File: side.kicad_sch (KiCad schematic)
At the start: 52 parts, among them SW1 SW_Push, SW10 SW_Push, SW11 SW_Push, SW12 SW_Push, SW13 SW_Push, SW14 SW_Push, SW15 SW_Push, SW16 SW_Push, SW17 SW_Push, SW18 SW_Push, SW19 SW_Push, SW2 SW_Push, SW20 SW_Push, SW22 SW_Push, SW3 SW_Push, SW4 SW_Push, SW5 SW_Push, SW6 SW_Push, SW7 SW_Push, SW8 SW_Push, SW9 SW_Push, U1 XIAO-nRF52840-SMD

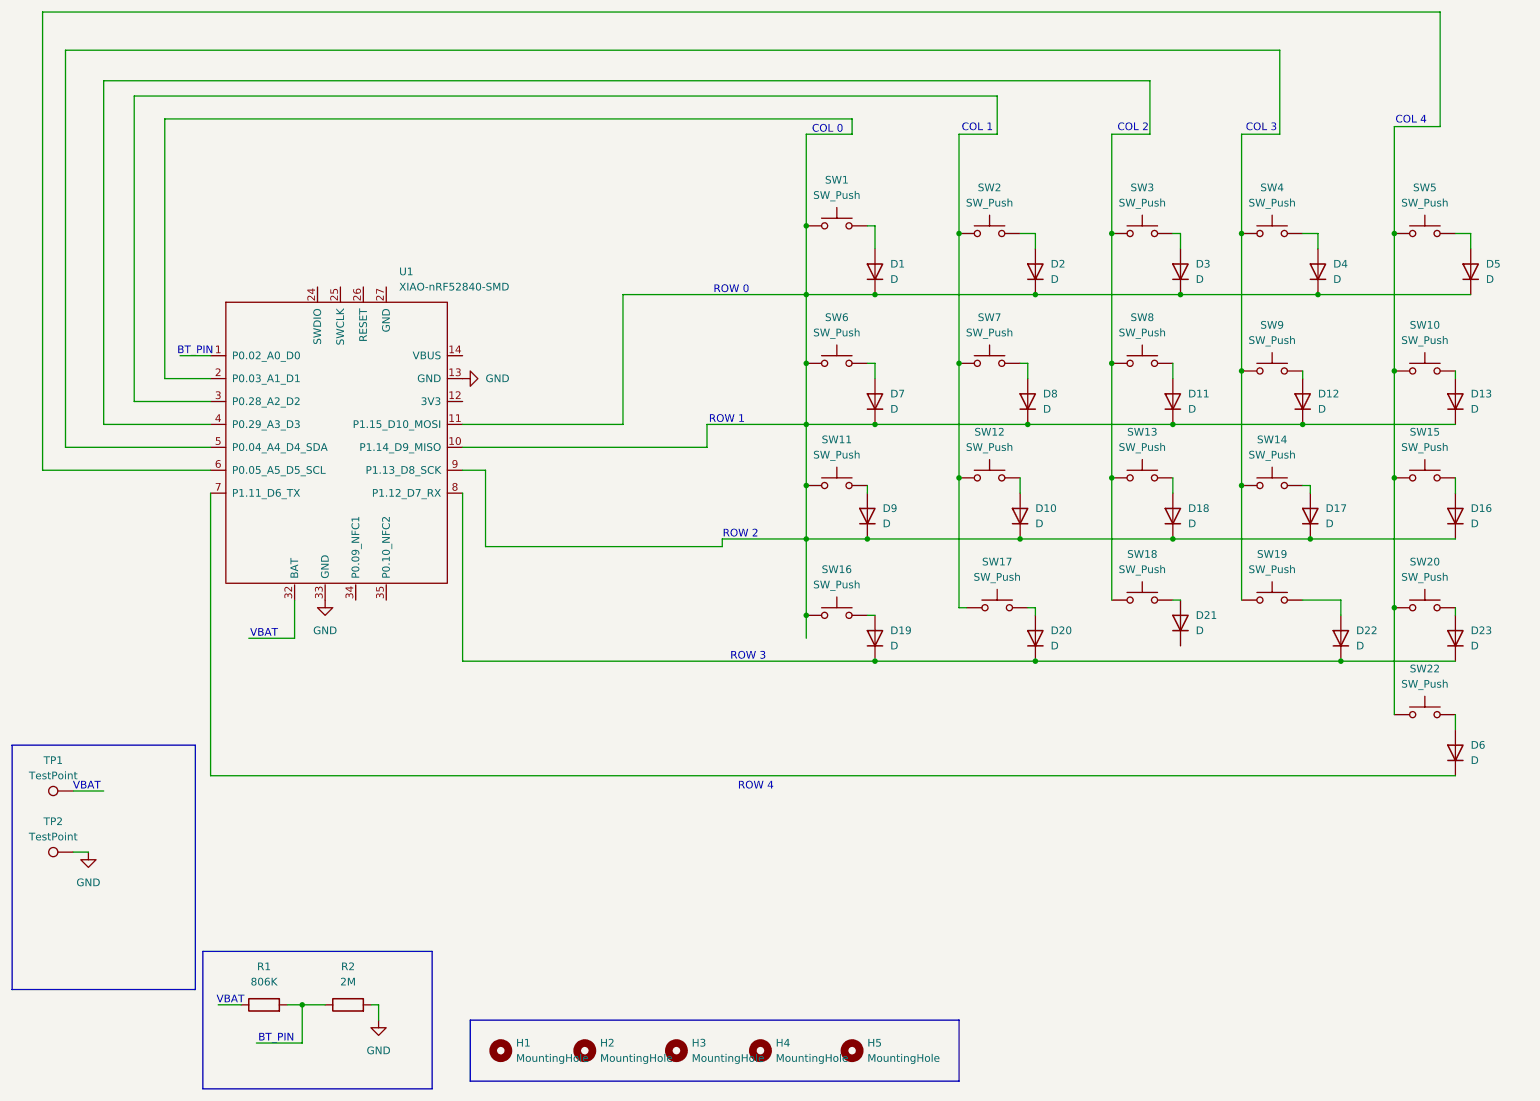
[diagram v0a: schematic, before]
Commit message: Rename schematic halves, update sheets and backups
Rename rightside.kicad_sch -> half.kicad_sch and lefthalf.kicad_sch -> side.kicad_sch; update sheet references, UUIDs, sheetfile names and sheet positions in kronos.kicad_sch and kronos.kicad_pro. Many symbol/text positions, junctions, wires and UUIDs were adjusted in the renamed/updated sheets to reflect the new layout. Clear used_designators in the project file. Rotate backup artifacts: remove two old kronos backups and add three new kronos-backups ZIPs; add ~kronos.kicad_pro.lck. This change reorganizes the schematic halves and updates project metadata and backups accordingly.
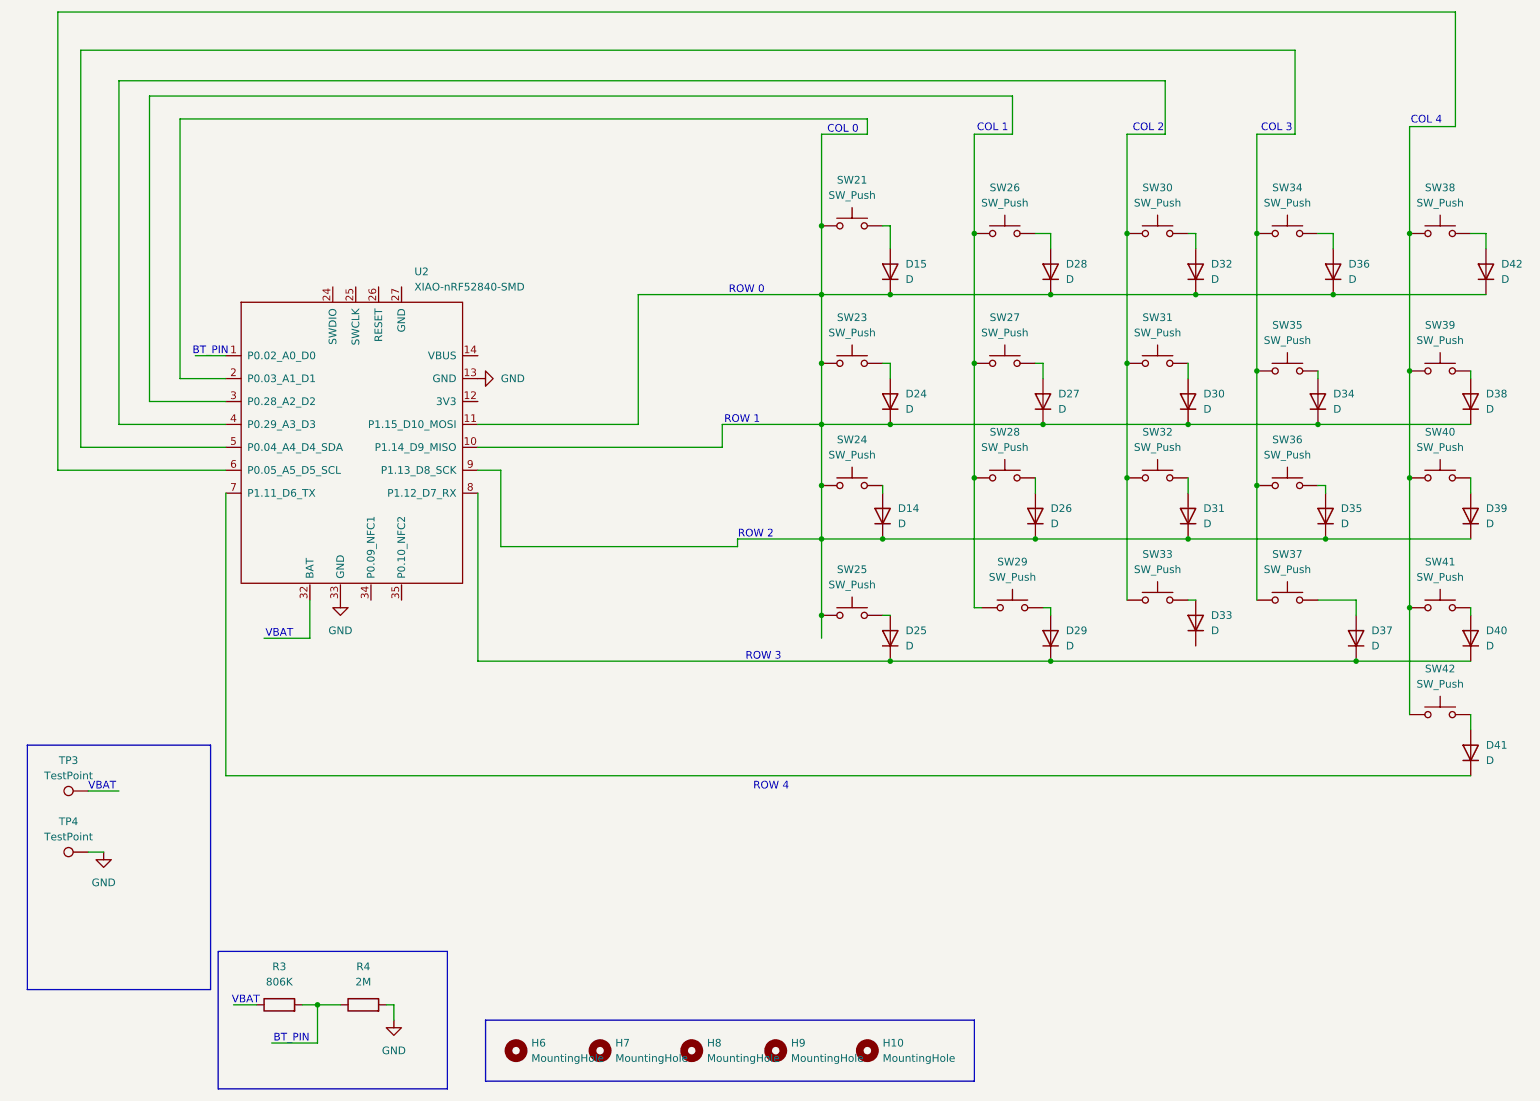
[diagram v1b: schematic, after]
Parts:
- removed D1, D10, D11, D12, D13, D16, D17, D18, D19, D2, D20, D21, D22, D23, D3, D4, D5, D6, D7, D8, D9: D, symbol Device:D
- removed H1, H2, H3, H4, H5: MountingHole, symbol Mechanical:MountingHole
- removed R1: 806K, symbol Device:R
- removed R2: 2M, symbol Device:R
- removed SW1, SW10, SW11, SW12, SW13, SW14, SW15, SW16, SW17, SW18, SW19, SW2, SW20, SW22, SW3, SW4, SW5, SW6, SW7, SW8, SW9: SW_Push, symbol Switch:SW_Push
- removed TP1, TP2: TestPoint, symbol Connector:TestPoint
- removed U1: XIAO-nRF52840-SMD, Seeed_Studio_XIAO_Series:XIAO-nRF52840-SMD, symbol Seeed_Studio_XIAO_Series:XIAO-nRF52840-SMD
- added D14, D15, D24, D25, D26, D27, D28, D29, D30, D31, D32, D33, D34, D35, D36, D37, D38, D39, D40, D41, D42: D, Diode_SMD:D_SOD-123, symbol Device:D
- added H10, H6, H7, H8, H9: MountingHole, symbol Mechanical:MountingHole
- added R3: 806K, Resistor_SMD:R_0805_2012Metric, symbol Device:R
- added R4: 2M, Resistor_SMD:R_0805_2012Metric, symbol Device:R
- added SW21, SW23, SW24, SW25, SW26, SW27, SW28, SW29, SW30, SW31, SW32, SW33, SW34, SW35, SW36, SW37, SW38, SW39, SW40, SW41, SW42: SW_Push, symbol Switch:SW_Push
- added TP3, TP4: TestPoint, TestPoint:TestPoint_Pad_D2.0mm, symbol Connector:TestPoint
- added U2: XIAO-nRF52840-SMD, kronoschems:modified-XIAO-nRF52840-SMD, symbol Seeed_Studio_XIAO_Series:XIAO-nRF52840-SMD
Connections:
- net GND: now also R4.2, TP4.1, U2.13 (GND), U2.33 (GND)
- new net: D14.1 (K), D15.1 (K), D24.1 (K), D26.1 (K), D27.1 (K), D28.1 (K), D30.1 (K), D31.1 (K), D32.1 (K), D34.1 (K), D35.1 (K), D36.1 (K), D38.1 (K), D39.1 (K), D42.1 (K), SW21.1, SW23.1, SW24.1, SW25.1, U2.10 (P1.14_D9_MISO), U2.11 (P1.15_D10_MOSI), U2.2 (P0.03_A1_D1), U2.9 (P1.13_D8_SCK)
- new net: D42.2 (A), SW38.2
- new net: SW34.1, SW35.1, SW36.1, SW37.1, U2.5 (P0.04_A4_D4_SDA)
- new net: D35.2 (A), SW36.2
- new net: D33.2 (A), SW33.2
- new net: D14.2 (A), SW24.2
- new net: SW30.1, SW31.1, SW32.1, SW33.1, U2.4 (P0.29_A3_D3)
- new net: D30.2 (A), SW31.2
- new net: D32.2 (A), SW30.2
- new net: D41.1 (K), U2.7 (P1.11_D6_TX)
- new net: D41.2 (A), SW42.2
- new net: SW26.1, SW27.1, SW28.1, SW29.1, U2.3 (P0.28_A2_D2)
- new net: SW38.1, SW39.1, SW40.1, SW41.1, SW42.1, U2.6 (P0.05_A5_D5_SCL)
- new net: D25.1 (K), D29.1 (K), D37.1 (K), D40.1 (K), U2.8 (P1.12_D7_RX)
- new net: D26.2 (A), SW28.2
- new net: D15.2 (A), SW21.2
- new net: D39.2 (A), SW40.2
- new net: R3.2, R4.1
- new net: D38.2 (A), SW39.2
- new net: D37.2 (A), SW37.2
- new net: D27.2 (A), SW27.2
- new net: D25.2 (A), SW25.2
- new net: D40.2 (A), SW41.2
- new net: D24.2 (A), SW23.2
- new net: D34.2 (A), SW35.2
- new net: D31.2 (A), SW32.2
- new net: D29.2 (A), SW29.2
- new net: D28.2 (A), SW26.2
- new net: D36.2 (A), SW34.2

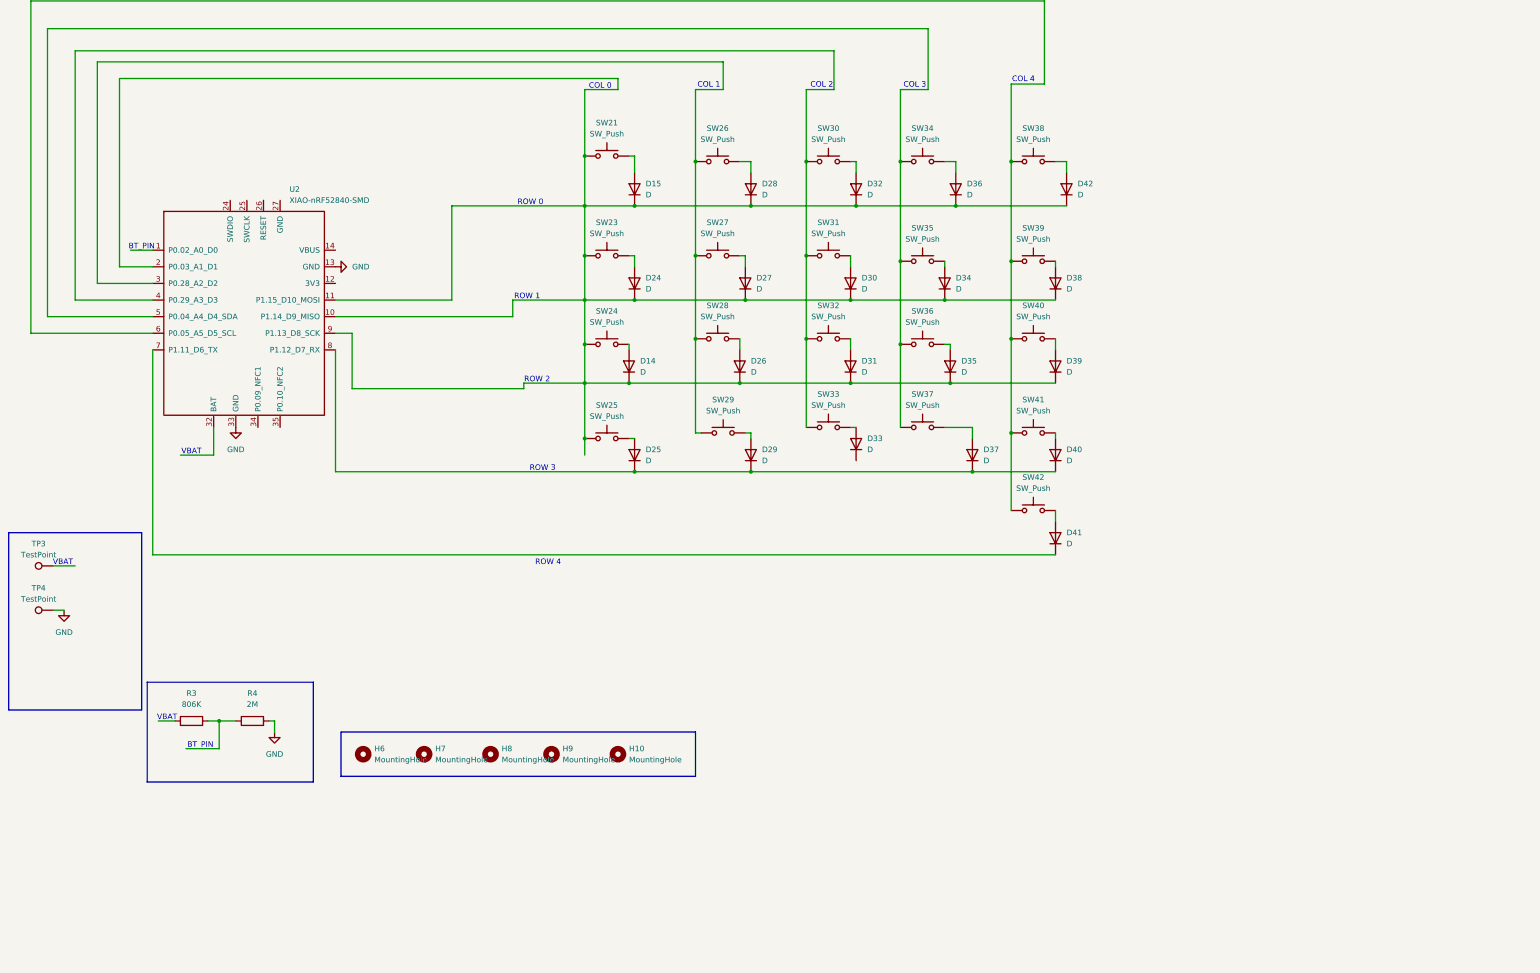
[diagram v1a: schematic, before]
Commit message: Update kronos PCB and add backups
Add 11 kronos backup archives to kronos-backups/ and update kronos.kicad_pcb with expanded PCB data (layers, setup, footprints, pads and components). Also update project files kronos.kicad_prl, kronos.kicad_pro and side.kicad_sch. These changes capture a saved PCB layout revision and store multiple timestamped backups.
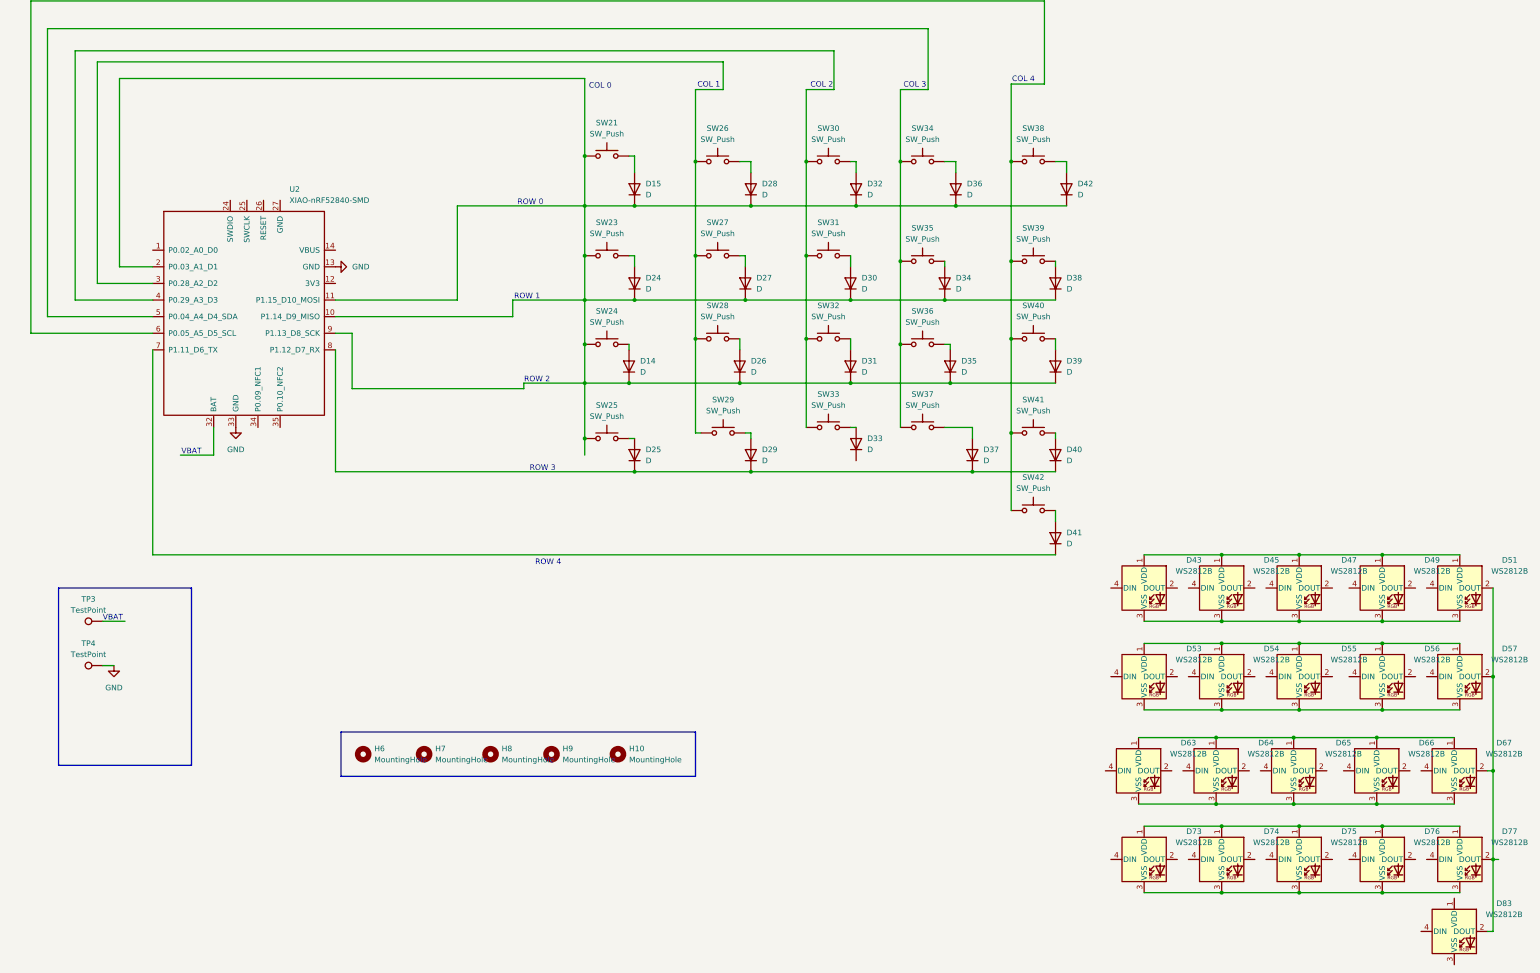
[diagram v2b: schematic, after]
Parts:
- removed R3: 806K, Resistor_SMD:R_0805_2012Metric, symbol Device:R
- removed R4: 2M, Resistor_SMD:R_0805_2012Metric, symbol Device:R
- added D43, D45, D47, D49, D51, D53, D54, D55, D56, D57, D63, D64, D65, D66, D67, D73, D74, D75, D76, D77, D83: WS2812B, LED_SMD:LED_WS2812B_PLCC4_5.0x5.0mm_P3.2mm, symbol LED:WS2812B
- H10, H6, H7, H8, H9: footprint (none) -> kronoschems:mouse-bite-5mm-slot
- SW21, SW23, SW24, SW25, SW26, SW27, SW28, SW29, SW30, SW31, SW32, SW33, SW34, SW35, SW36, SW37, SW38, SW39, SW40, SW41, SW42: footprint (none) -> PCM_marbastlib-mx:SW_MX_HS_KS-2P02B01-01_1u
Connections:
- new net: D53.1 (VDD), D54.1 (VDD), D55.1 (VDD), D56.1 (VDD), D57.1 (VDD)
- new net: D53.3 (VSS), D54.3 (VSS), D55.3 (VSS), D56.3 (VSS), D57.3 (VSS)
- new net: D43.1 (VDD), D45.1 (VDD), D47.1 (VDD), D49.1 (VDD), D51.1 (VDD)
- new net: D43.3 (VSS), D45.3 (VSS), D47.3 (VSS), D49.3 (VSS), D51.3 (VSS)
- new net: D51.2 (DOUT), D57.2 (DOUT), D67.2 (DOUT), D77.2 (DOUT), D83.2 (DOUT)
- new net: D73.1 (VDD), D74.1 (VDD), D75.1 (VDD), D76.1 (VDD), D77.1 (VDD)
- new net: D73.3 (VSS), D74.3 (VSS), D75.3 (VSS), D76.3 (VSS), D77.3 (VSS)
- new net: D63.1 (VDD), D64.1 (VDD), D65.1 (VDD), D66.1 (VDD), D67.1 (VDD)
- new net: D63.3 (VSS), D64.3 (VSS), D65.3 (VSS), D66.3 (VSS), D67.3 (VSS)
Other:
- note removed: "BT_PIN"
- moved on the sheet: TP3, TP4

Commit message: PCB akmost done
PCB added; scheme update; blah blah
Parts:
- removed D43, D45, D47, D49, D51, D53, D54, D55, D56, D57, D63, D64, D65, D66, D67, D73, D74, D75, D76, D77, D83: WS2812B, LED_SMD:LED_WS2812B_PLCC4_5.0x5.0mm_P3.2mm, symbol LED:WS2812B
- removed U2: XIAO-nRF52840-SMD, kronoschems:modified-XIAO-nRF52840-SMD, symbol Seeed_Studio_XIAO_Series:XIAO-nRF52840-SMD
- added D101, D103, D104, D106, D113, D114, D116, D117, D118, D126, D86, D87, D89, D90, D91, D93, D94, D95, D97, D98, D99: WS2812B, LED_SMD:LED_WS2812B_PLCC4_5.0x5.0mm_P3.2mm, symbol LED:WS2812B
- added U3: Seeeduino Xiao nRF52840, PCM_marbastlib-xp-promicroish:Xiao_nRF52840_ACH, symbol PCM_marbastlib-promicroish:Seeeduino_Xiao_nRF52840
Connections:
- net GND: now also D101.3 (VSS), D103.3 (VSS), D104.3 (VSS), D106.3 (VSS), D113.3 (VSS), D114.3 (VSS), D116.3 (VSS), D117.3 (VSS), D118.3 (VSS), D126.3 (VSS), D86.3 (VSS), D87.3 (VSS), D89.3 (VSS), D90.3 (VSS), D91.3 (VSS), D93.3 (VSS), D94.3 (VSS), D95.3 (VSS), D97.3 (VSS), D98.3 (VSS), D99.3 (VSS), U3.15 (BAT-), U3.9 (GND)
- net at D14.1 (K), D15.1 (K), D24.1 (K)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: now also U3.11 (P1.15), U3.12 (P1.14), U3.13 (P1.13), U3.2 (P0.03)
- net at SW34.1, SW35.1, SW36.1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: now also U3.5 (P0.04)
- net at D33.1 (K): now also D25.1 (K), D29.1 (K), D37.1 (K), D40.1 (K), U3.14 (P1.12)
- net at SW30.1, SW31.1, SW32.1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: now also U3.4 (P0.29)
- net at D41.1 (K): now also U3.7 (P1.11)
- net at SW26.1, SW27.1, SW28.1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: now also U3.3 (P0.28)
- net at SW38.1, SW39.1, SW40.1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: now also U3.6 (P0.05)
- new net: D95.2 (DOUT), D99.4 (DIN)
- new net: D91.2 (DOUT), D95.4 (DIN)
- new net: D113.2 (DOUT), D114.4 (DIN)
- new net: D113.4 (DIN), U3.1 (P0.02)
- new net: D114.2 (DOUT), D116.4 (DIN)
- new net: D106.2 (DOUT), D126.4 (DIN)
- new net: D101.2 (DOUT), D106.4 (DIN)
- new net: D104.2 (DOUT), D89.4 (DIN)
- new net: D104.4 (DIN), D99.2 (DOUT)
- new net: D116.2 (DOUT), D117.4 (DIN)
- new net: D93.2 (DOUT), D97.4 (DIN)
- new net: D89.2 (DOUT), D93.4 (DIN)
- new net: D87.2 (DOUT), D91.4 (DIN)
- new net: D103.2 (DOUT), D87.4 (DIN)
- new net: D103.4 (DIN), D98.2 (DOUT)
- new net: D101.4 (DIN), D97.2 (DOUT)
- new net: D118.2 (DOUT), D86.4 (DIN)
- new net: D117.2 (DOUT), D118.4 (DIN)
- new net: D90.2 (DOUT), D94.4 (DIN)
- new net: D86.2 (DOUT), D90.4 (DIN)
- new net: D94.2 (DOUT), D98.4 (DIN)
- new net +5V: D101.1 (VDD), D103.1 (VDD), D104.1 (VDD), D106.1 (VDD), D113.1 (VDD), D114.1 (VDD), D116.1 (VDD), D117.1 (VDD), D118.1 (VDD), D126.1 (VDD), D86.1 (VDD), D87.1 (VDD), D89.1 (VDD), D90.1 (VDD), D91.1 (VDD), D93.1 (VDD), D94.1 (VDD), D95.1 (VDD), D97.1 (VDD), D98.1 (VDD), D99.1 (VDD)
- no-connect marks 0 -> 9
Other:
- moved on the sheet: D33
